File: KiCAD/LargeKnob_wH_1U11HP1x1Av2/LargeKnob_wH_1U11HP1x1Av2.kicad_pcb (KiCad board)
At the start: 2 copper layers, 55.5 x 39.7 mm, 6 parts

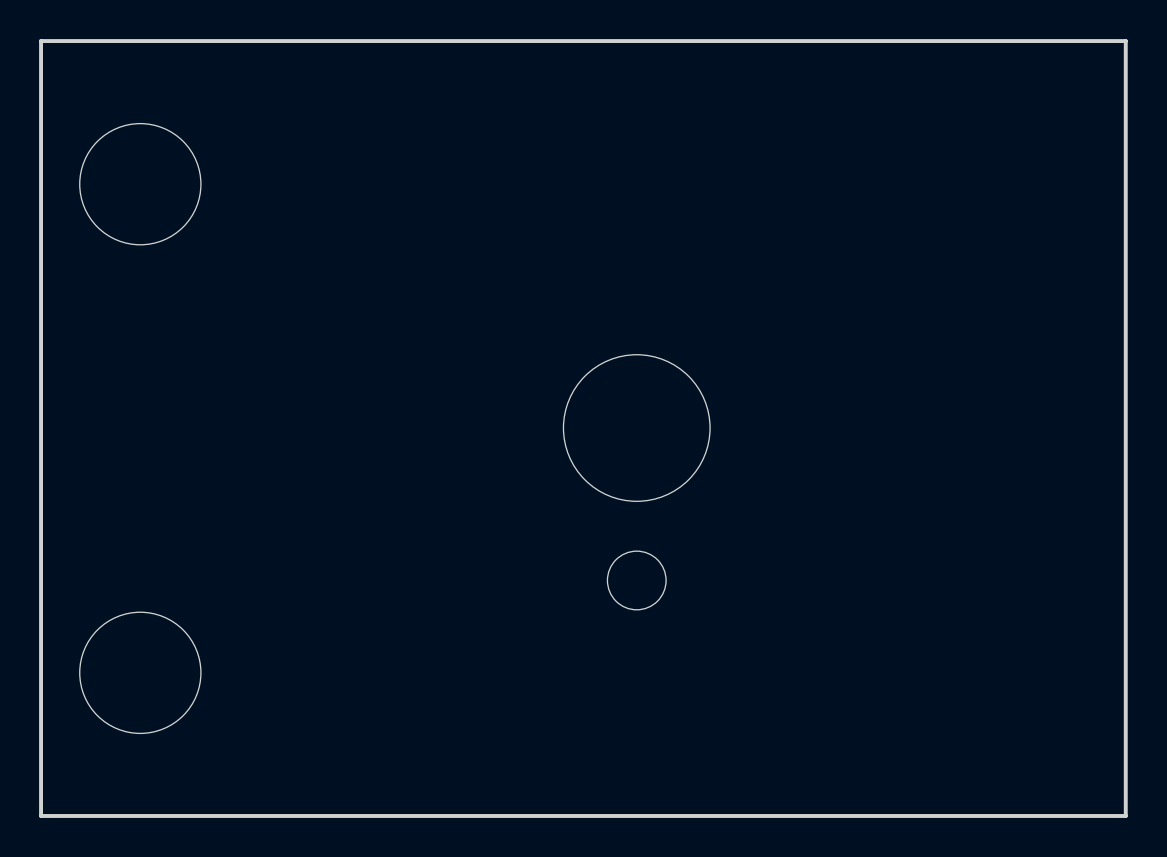
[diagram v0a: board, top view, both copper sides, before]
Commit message: updated all modules to use plated through-holes wherever possible
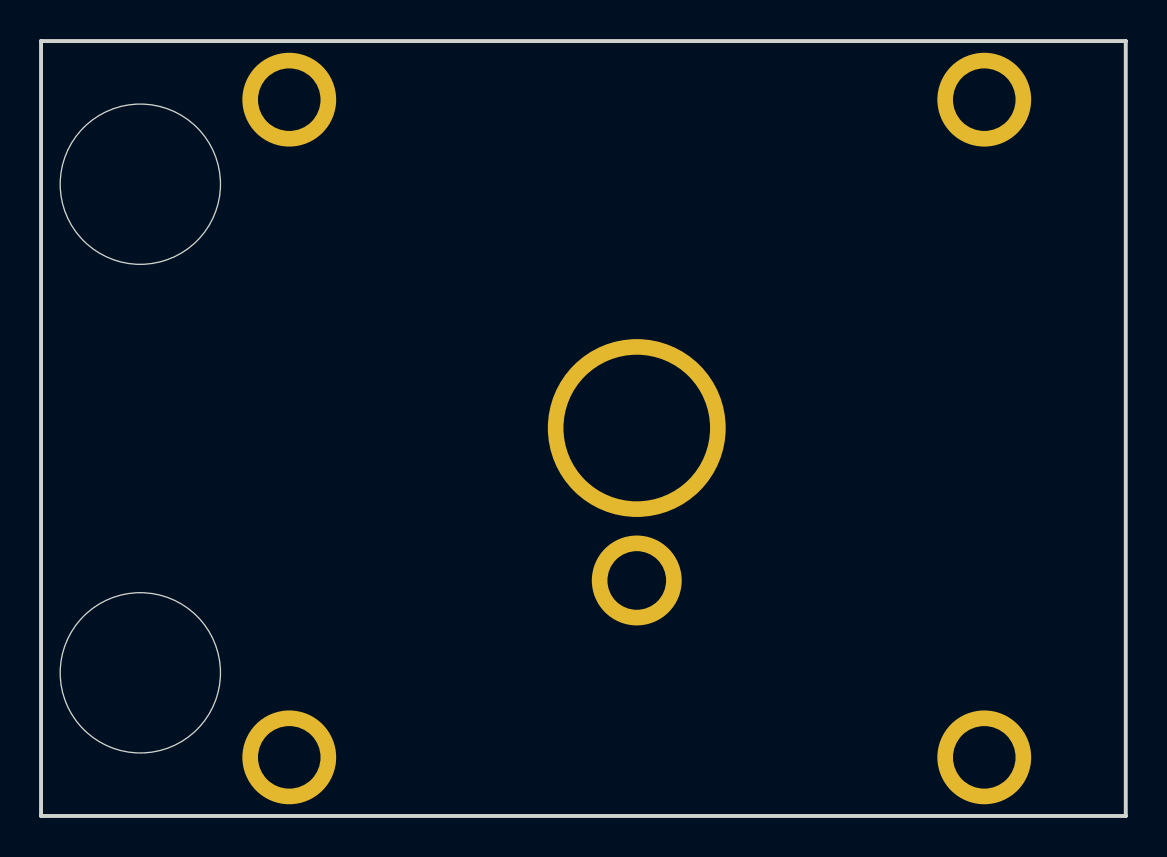
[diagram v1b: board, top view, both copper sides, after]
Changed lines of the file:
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@@
 			)
 		)
-		(pad "" np_thru_hole oval
+		(pad "" thru_hole circle
 			(at 0 0)
-			(size 4.34 3.2)
-			(drill oval 4.34 3.2)
-			(layers "*.Cu" "*.Mask")
+			(size 4.8 4.8)
+			(drill 3.2)
+			(layers "*.Cu" "*.Mask")
+			(remove_unused_layers no)
 		)
 		(embedded_fonts no)
@@
 			)
 		)
-		(pad "" np_thru_hole oval
+		(pad "" thru_hole circle
 			(at 0 0)
-			(size 4.34 3.2)
-			(drill oval 4.34 3.2)
-			(layers "*.Cu" "*.Mask")
+			(size 4.8 4.8)
+			(drill 3.2)
+			(layers "*.Cu" "*.Mask")
+			(remove_unused_layers no)
 		)
 		(embedded_fonts no)
@@
 			)
 		)
-		(pad "" np_thru_hole oval
+		(pad "" thru_hole circle
 			(at 0 0)
-			(size 4.34 3.2)
-			(drill oval 4.34 3.2)
-			(layers "*.Cu" "*.Mask")
+			(size 4.8 4.8)
+			(drill 3.2)
+			(layers "*.Cu" "*.Mask")
+			(remove_unused_layers no)
 		)
 		(embedded_fonts no)
@@
 		(at 30.48 22.225)
 		(property "Reference" "RP1"
-			(at 0 -4.75 0)
+			(at 0.02 -5.975 0)
 			(unlocked yes)
 			(layer "B.SilkS")
@@
 		)
 		(property "Value" "M7_Panel_Mount_Rotary_Potentiometer"
-			(at 0 10 0)
+			(at 0.02 11.275 0)
 			(unlocked yes)
 			(layer "F.Fab")
@@
 		)
 		(fp_text user "${REFERENCE}"
-			(at 0 -4.75 0)
-			(unlocked yes)
-			(layer "F.Fab")
-			(effects
-				(font
-					(size 1 1)
-					(thickness 0.15)
-				)
-			)
-		)
-		(pad "" np_thru_hole circle
+			(at 0.02 -5.975 0)
+			(unlocked yes)
+			(layer "F.Fab")
+			(effects
+				(font
+					(size 1 1)
+					(thickness 0.15)
+				)
+			)
+		)
+		(pad "" thru_hole circle
 			(at 0 0)
-			(size 7.5 7.5)
+			(size 9.1 9.1)
 			(drill 7.5)
 			(layers "*.Cu" "*.Mask")
-		)
-		(pad "" np_thru_hole circle
+			(remove_unused_layers no)
+		)
+		(pad "" thru_hole circle
 			(at 0 7.8)
-			(size 3 3)
+			(size 4.6 4.6)
 			(drill 3)
 			(layers "*.Cu" "*.Mask")
+			(remove_unused_layers no)
 		)
 		(embedded_fonts no)
@@
 			)
 		)
-		(pad "" np_thru_hole oval
+		(pad "" thru_hole circle
 			(at 0 0)
-			(size 4.34 3.2)
-			(drill oval 4.34 3.2)
-			(layers "*.Cu" "*.Mask")
+			(size 4.8 4.8)
+			(drill 3.2)
+			(layers "*.Cu" "*.Mask")
+			(remove_unused_layers no)
 		)
 		(embedded_fonts no)
@@
 		(at 5.08 9.75)
 		(property "Reference" "H5"
-			(at 0 -4 0)
+			(at 0 -5.25 0)
 			(unlocked yes)
 			(layer "B.SilkS")
@@
 		(fp_circle
 			(center 0 0)
-			(end 3.1 0)
+			(end 4.1 0)
 			(stroke
 				(width 0.2)
@@
 		(fp_circle
 			(center 0 25)
-			(end 3.1 25)
+			(end 4.1 25)
 			(stroke
 				(width 0.2)
@@
 		(pad "" np_thru_hole circle
 			(at 0 0)
-			(size 6.2 6.2)
-			(drill 6.2)
+			(size 8.2 8.2)
+			(drill 8.2)
 			(layers "*.Cu" "*.Mask")
 		)
 		(pad "" np_thru_hole circle
 			(at 0 25)
-			(size 6.2 6.2)
-			(drill 6.2)
-			(layers "*.Cu" "*.Mask")
-		)
+			(size 8.2 8.2)
+			(drill 8.2)
+			(layers "*.Cu" "*.Mask")
+		)
